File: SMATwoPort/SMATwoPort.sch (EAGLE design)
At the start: 3 parts

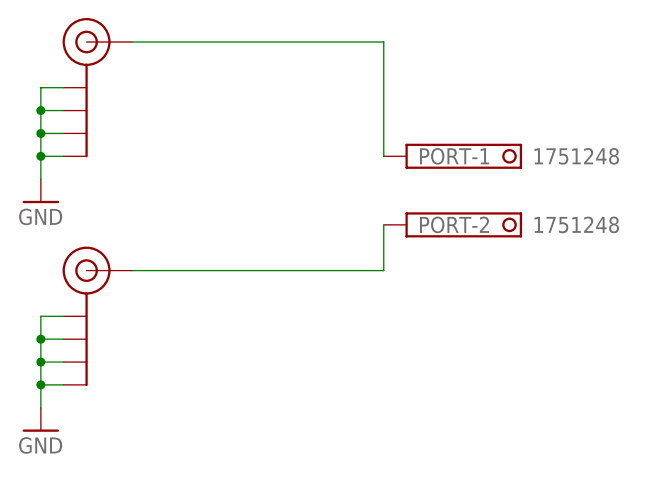
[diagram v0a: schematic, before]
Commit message: Updated pcb to have sma's on the side to accommodate Network Analyzer cables.
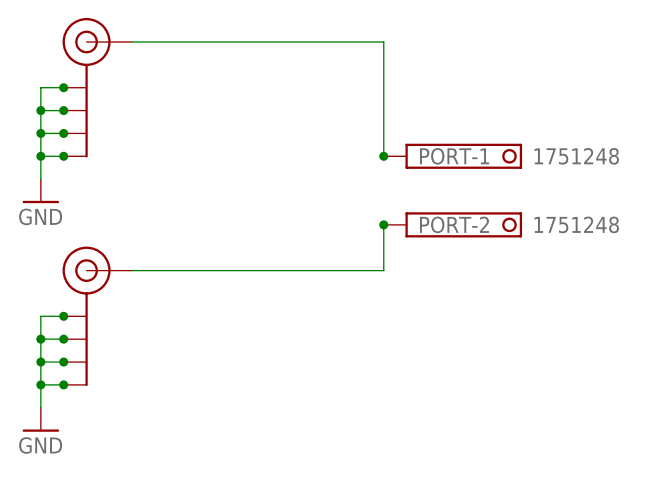
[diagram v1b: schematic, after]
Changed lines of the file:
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@@
 <?xml version="1.0" encoding="utf-8"?>
 <!DOCTYPE eagle SYSTEM "eagle.dtd">
-<eagle version="7.4.0">
+<eagle version="7.2.0">
 <drawing>
 <settings>
@@
 </busses>
 <nets>
-<net name="N$3" class="0">
-<segment>
-<pinref part="J$1" gate="1" pin="SIGNAL"/>
-<pinref part="PORT" gate="-2" pin="K"/>
-<wire x1="58.42" y1="38.1" x2="58.42" y2="33.02" width="0.1524" layer="91"/>
-<wire x1="58.42" y1="33.02" x2="30.48" y2="33.02" width="0.1524" layer="91"/>
-</segment>
-</net>
-<net name="N$4" class="0">
+<net name="N$1" class="0">
 <segment>
 <pinref part="J$2" gate="1" pin="SIGNAL"/>
@@
 <wire x1="30.48" y1="58.42" x2="58.42" y2="58.42" width="0.1524" layer="91"/>
 <wire x1="58.42" y1="58.42" x2="58.42" y2="45.72" width="0.1524" layer="91"/>
+<junction x="58.42" y="45.72"/>
+</segment>
+</net>
+<net name="N$2" class="0">
+<segment>
+<pinref part="J$1" gate="1" pin="SIGNAL"/>
+<pinref part="PORT" gate="-2" pin="K"/>
+<wire x1="30.48" y1="33.02" x2="58.42" y2="33.02" width="0.1524" layer="91"/>
+<wire x1="58.42" y1="33.02" x2="58.42" y2="38.1" width="0.1524" layer="91"/>
+<junction x="58.42" y="38.1"/>
 </segment>
 </net>
@@
 <wire x1="20.32" y1="45.72" x2="20.32" y2="43.18" width="0.1524" layer="91"/>
 <wire x1="22.86" y1="50.8" x2="20.32" y2="50.8" width="0.1524" layer="91"/>
-<junction x="20.32" y="50.8"/>
 <pinref part="J$2" gate="1" pin="GND@2"/>
 <wire x1="22.86" y1="48.26" x2="20.32" y2="48.26" width="0.1524" layer="91"/>
-<junction x="20.32" y="48.26"/>
 <pinref part="J$2" gate="1" pin="GND@3"/>
 <wire x1="22.86" y1="45.72" x2="20.32" y2="45.72" width="0.1524" layer="91"/>
+<junction x="22.86" y="53.34"/>
+<junction x="22.86" y="50.8"/>
+<junction x="22.86" y="48.26"/>
+<junction x="22.86" y="45.72"/>
 <junction x="20.32" y="45.72"/>
+<junction x="20.32" y="48.26"/>
+<junction x="20.32" y="50.8"/>
 </segment>
 <segment>
@@
 <wire x1="20.32" y1="20.32" x2="20.32" y2="17.78" width="0.1524" layer="91"/>
 <wire x1="22.86" y1="25.4" x2="20.32" y2="25.4" width="0.1524" layer="91"/>
-<junction x="20.32" y="25.4"/>
 <pinref part="J$1" gate="1" pin="GND@2"/>
 <wire x1="22.86" y1="22.86" x2="20.32" y2="22.86" width="0.1524" layer="91"/>
-<junction x="20.32" y="22.86"/>
 <pinref part="J$1" gate="1" pin="GND@3"/>
 <wire x1="22.86" y1="20.32" x2="20.32" y2="20.32" width="0.1524" layer="91"/>
+<junction x="20.32" y="25.4"/>
+<junction x="22.86" y="25.4"/>
+<junction x="22.86" y="27.94"/>
+<junction x="22.86" y="22.86"/>
+<junction x="20.32" y="22.86"/>
 <junction x="20.32" y="20.32"/>
+<junction x="22.86" y="20.32"/>
 </segment>
 </net>
